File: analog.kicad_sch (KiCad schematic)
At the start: 37 parts, among them J2 494_OUT, J3 POT, Q2 AO3400A, U1 TL494, U5 LM358

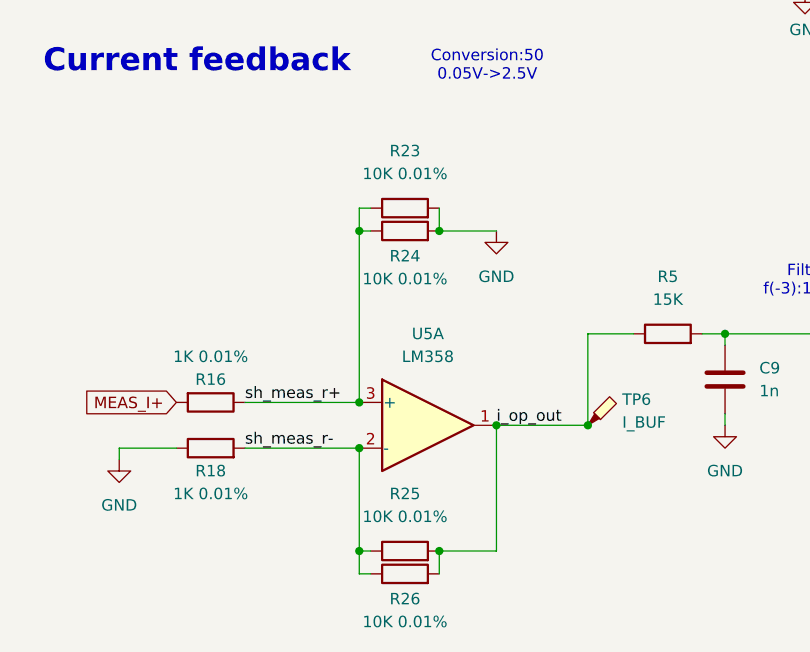
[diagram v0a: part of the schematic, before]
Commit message: changed OpAmp resistor values for i channel, top layer gnd filled zone
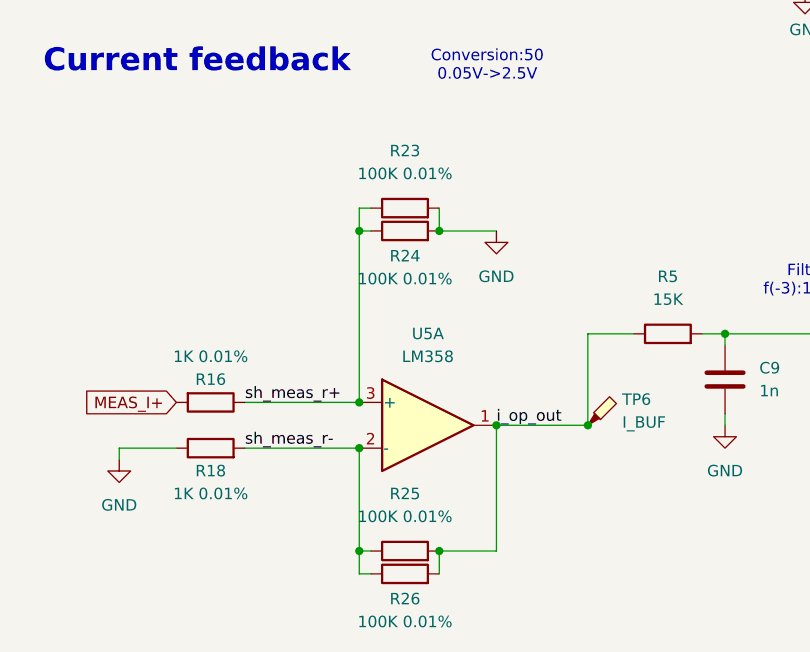
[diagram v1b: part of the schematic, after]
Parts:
- R23, R24, R25, R26: value 10K 0.01% -> 100K 0.01%; footprint Resistor_SMD:R_0805_2012Metric_Pad1.20x1.40mm_HandSolder -> Resistor_SMD:R_1206_3216Metric_Pad1.30x1.75mm_HandSolder
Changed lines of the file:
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@@
 			)
 		)
-		(property "Value" "10K 0.01%"
+		(property "Value" "100K 0.01%"
 			(at 62.23 131.064 90)
 			(effects
@@
 			)
 		)
-		(property "Footprint" "Resistor_SMD:R_0805_2012Metric_Pad1.20x1.40mm_HandSolder"
+		(property "Footprint" "Resistor_SMD:R_1206_3216Metric_Pad1.30x1.75mm_HandSolder"
 			(at 62.23 127.508 90)
 			(effects
@@
 			)
 		)
-		(property "Value" "10K 0.01%"
+		(property "Value" "100K 0.01%"
 			(at 62.23 157.48 90)
 			(effects
@@
 			)
 		)
-		(property "Footprint" "Resistor_SMD:R_0805_2012Metric_Pad1.20x1.40mm_HandSolder"
+		(property "Footprint" "Resistor_SMD:R_1206_3216Metric_Pad1.30x1.75mm_HandSolder"
 			(at 62.23 163.068 90)
 			(effects
@@
 			)
 		)
-		(property "Value" "10K 0.01%"
+		(property "Value" "100K 0.01%"
 			(at 62.23 169.164 90)
 			(effects
@@
 			)
 		)
-		(property "Footprint" "Resistor_SMD:R_0805_2012Metric_Pad1.20x1.40mm_HandSolder"
+		(property "Footprint" "Resistor_SMD:R_1206_3216Metric_Pad1.30x1.75mm_HandSolder"
 			(at 62.23 165.608 90)
 			(effects
@@
 			)
 		)
-		(property "Value" "10K 0.01%"
+		(property "Value" "100K 0.01%"
 			(at 62.23 119.38 90)
 			(effects
@@
 			)
 		)
-		(property "Footprint" "Resistor_SMD:R_0805_2012Metric_Pad1.20x1.40mm_HandSolder"
+		(property "Footprint" "Resistor_SMD:R_1206_3216Metric_Pad1.30x1.75mm_HandSolder"
 			(at 62.23 124.968 90)
 			(effects

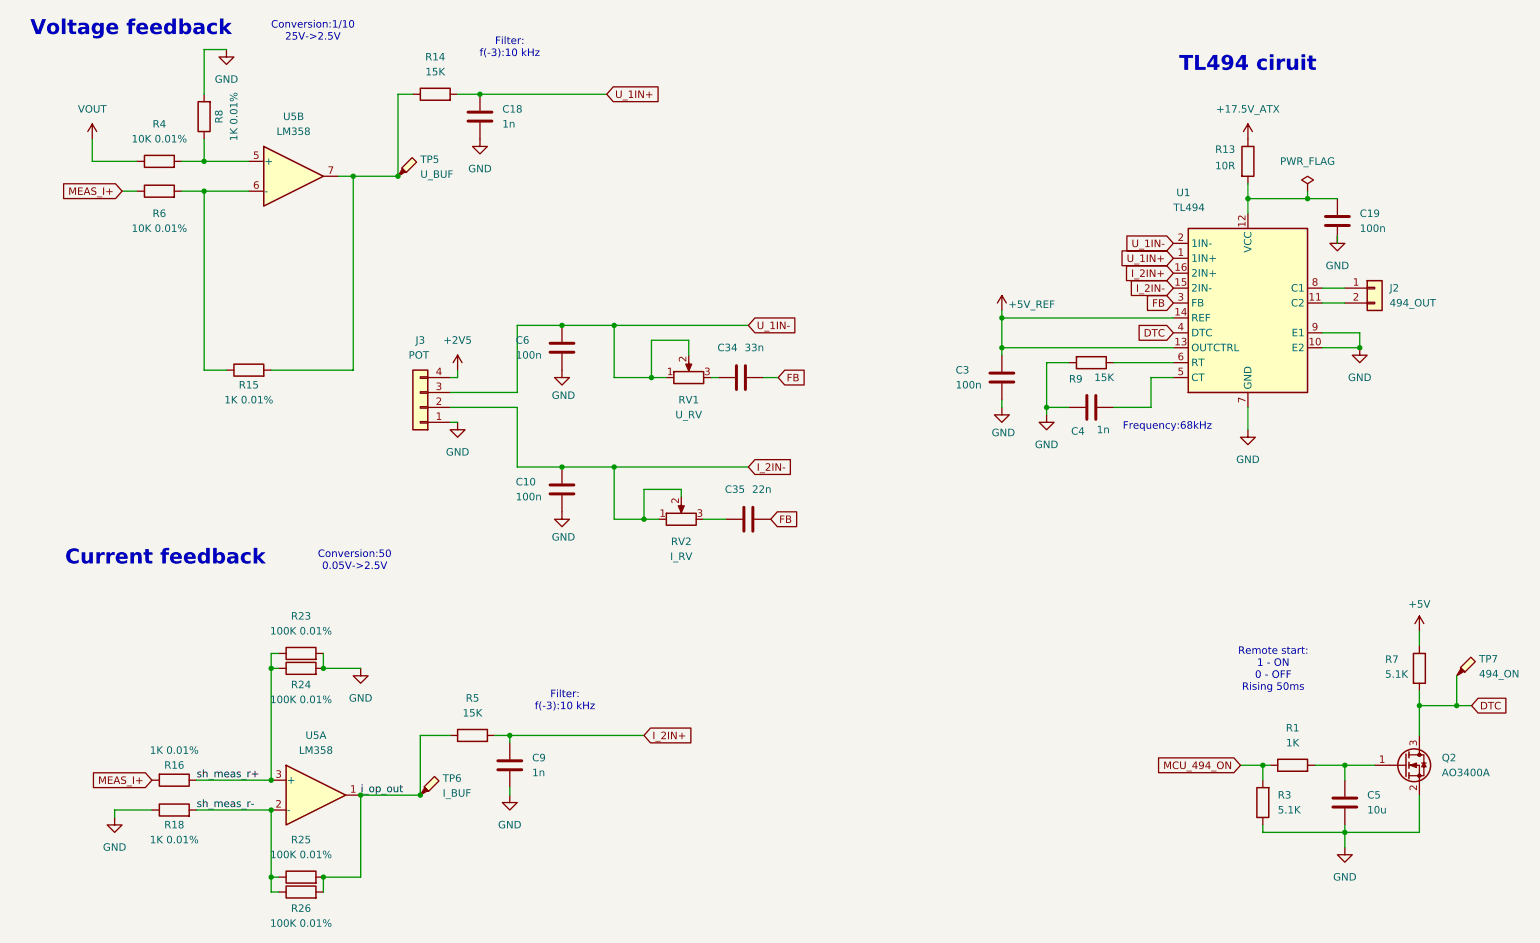
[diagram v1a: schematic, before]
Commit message: ref voltage from 2.5 to 5 V
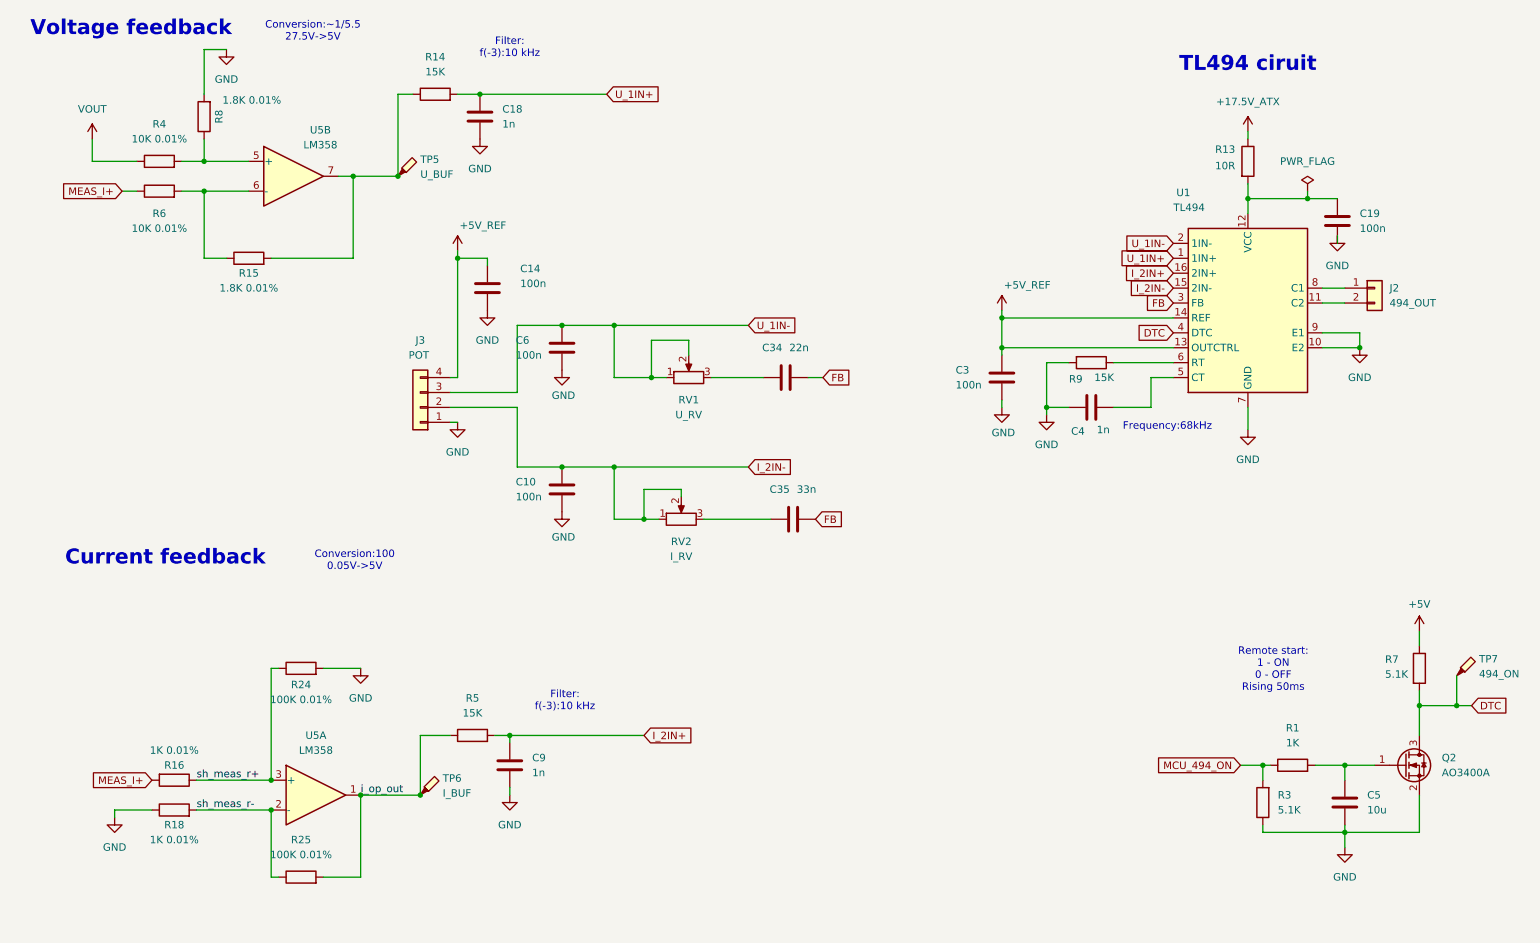
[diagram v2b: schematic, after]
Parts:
- removed R23, R26: 100K 0.01%, Resistor_SMD:R_1206_3216Metric_Pad1.30x1.75mm_HandSolder, symbol Device:R
- added C14: 100n, Capacitor_SMD:C_0805_2012Metric_Pad1.18x1.45mm_HandSolder, symbol Device:C
- C34: value 33n -> 22n
- C35: value 22n -> 33n
- R15, R8: value 1K 0.01% -> 1.8K 0.01%
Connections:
- net +2V5 is gone; now on net +5V_REF: J3.4 (Pin_4)
- net +5V_REF: now also C14.1
- net GND: now also C14.2
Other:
- note added: "Conversion:100 0.05V->5V"
- note added: "Conversion:~1/5.5 27.5V->5V"
- note removed: "Conversion:1/10 25V->2.5V"
- note removed: "Conversion:50 0.05V->2.5V"
- moved on the sheet: C34, C35, R15
